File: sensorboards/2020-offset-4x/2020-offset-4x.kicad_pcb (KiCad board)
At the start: 2 copper layers, 20.5 x 45.2 mm, 4 parts, among them J1 Conn_01x06_Male, U1 CNY70, U2 CNY70

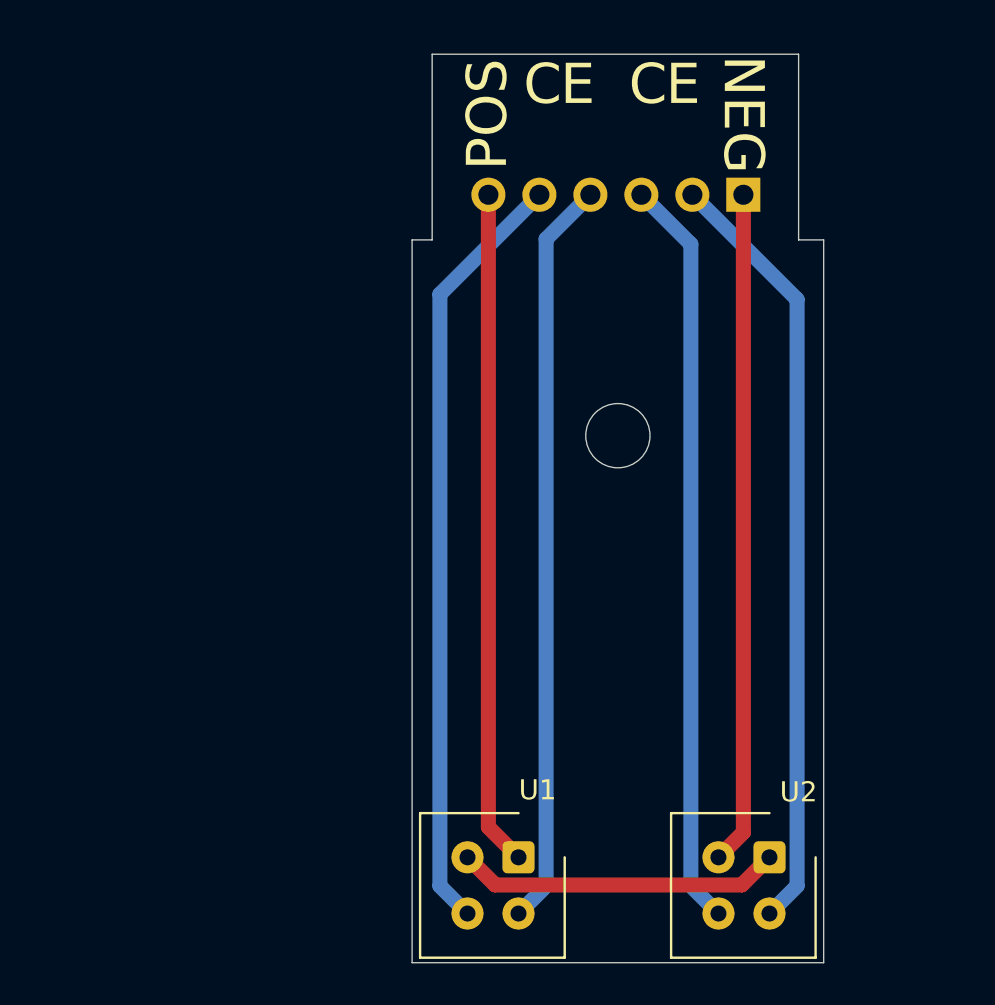
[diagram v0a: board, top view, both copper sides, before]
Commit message: Update 4x boards for issue #44; introduce the 12deg rotated hammer board
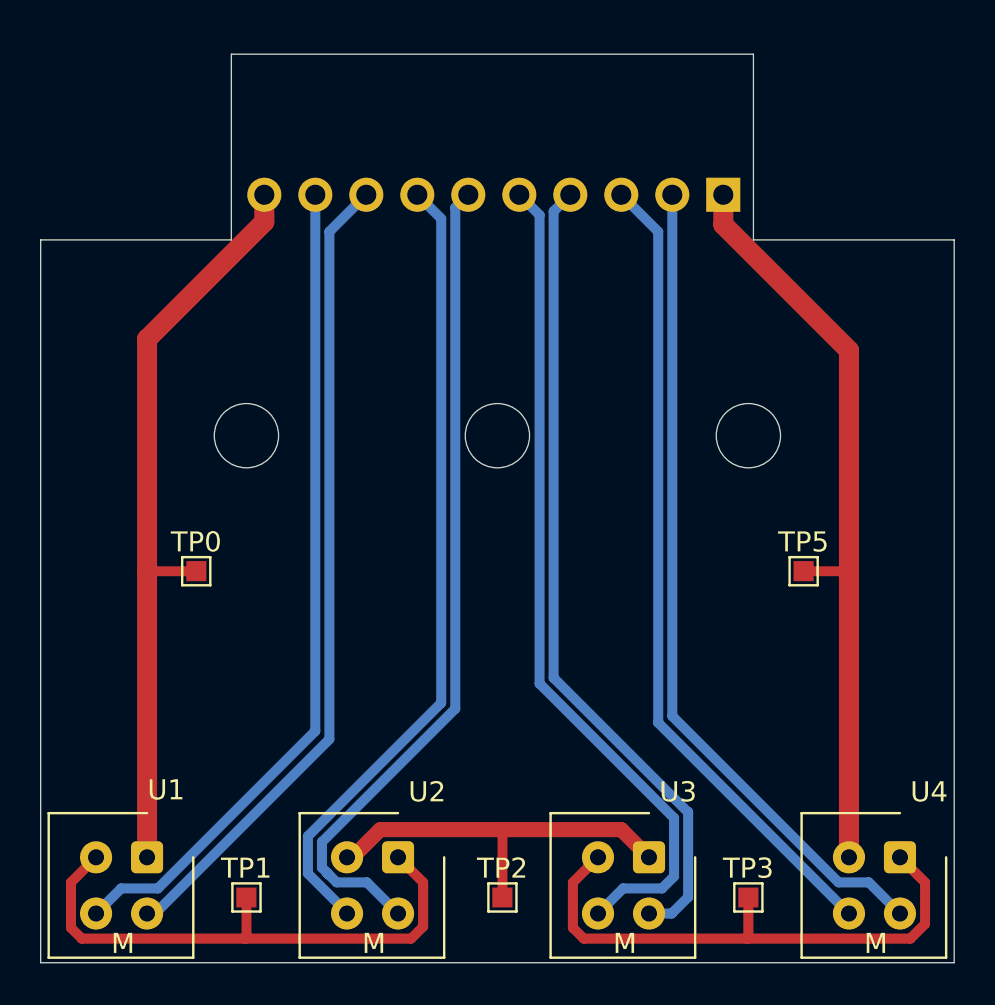
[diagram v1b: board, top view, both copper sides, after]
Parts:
- added H2: MountingHole, Mounting_Holes:MountingHole_3.2mm_M3, F.Cu at (175.2, 110.0)
- added H3: MountingHole, Mounting_Holes:MountingHole_3.2mm_M3, F.Cu at (187.8, 110.0)
- added TP0: TestPoint, TestPoint:TestPoint_Pad_1.0x1.0mm, F.Cu at (160.2, 116.8)
- added TP1: TestPoint, TestPoint:TestPoint_Pad_1.0x1.0mm, F.Cu at (162.8, 133.0)
- added TP2: TestPoint, TestPoint:TestPoint_Pad_1.0x1.0mm, F.Cu at (175.5, 133.0)
- added TP3: TestPoint, TestPoint:TestPoint_Pad_1.0x1.0mm, F.Cu at (187.8, 133.0)
- added TP5: TestPoint, TestPoint:TestPoint_Pad_1.0x1.0mm, F.Cu at (190.5, 116.8)
- added U3: CNY70, OptoDevice:Vishay_CNY70, F.Cu at (182.8, 131.0)
- added U4: CNY70, OptoDevice:Vishay_CNY70, F.Cu at (195.3, 131.0)
- J1: value Conn_01x06_Male -> Conn_01x10_Male; footprint Pin_Headers:Pin_Header_Angled_1x06_Pitch2.54mm -> Pin_Headers:Pin_Header_Angled_1x10_Pitch2.54mm
- moved H1 18.5 mm to (162.8, 110.0)
- moved U1 18.5 mm to (157.8, 131.0)
- moved U2 18.5 mm to (170.3, 131.0)
- moved J1 1.00 mm to (186.5, 98.0)
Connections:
- J1 pad 2: /E2 -> /E4
- J1 pad 3: /C2 -> /C4
- J1 pad 4: /E1 -> /E3
- J1 pad 5: /C1 -> /C3
- J1 pad 6: /POS -> /E2
- U2 pad 2: /NEG -> Net-(U2-Pad2)
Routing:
- net /C3: track 0.00 -> 41.7 mm
- net /E4: track 0.00 -> 41.4 mm
- net /C4: track 0.00 -> 40.5 mm
- net /E3: track 0.00 -> 40.4 mm
- net Net-(U3-Pad2): track 0.00 -> 28.0 mm
- net Net-(U2-Pad2): track 0.00 -> 19.6 mm
- net Net-(U1-Pad2): track 16.2 -> 28.1 mm
- net /NEG: track 33.5 -> 38.0 mm
- net /POS: track 33.6 -> 37.9 mm
- net /E1: track 37.3 -> 40.6 mm
- net /E2: track 38.5 -> 41.6 mm
- net /C1: track 38.4 -> 41.4 mm
- net /C2: track 37.4 -> 39.9 mm
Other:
- board size 20.5 x 45.2 mm -> 45.5 x 45.2 mm
- net class Default removed
- board text added: "Per Github issue #44, the power and signal traces have been made non-overlapping. I've decided to skip the addition of ground pours and electrically-connected mounting holes."
